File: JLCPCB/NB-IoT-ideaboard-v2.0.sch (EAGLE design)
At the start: 111 parts, among them Q1 32.768kHz, Q3 9013, Q4 9013, Q5 9013, U1 STM32F103RBT6, U2 MCP73831T-2ACI/OT, U3 AP2112-3.3, U4 PAM2401, U5 MICROSIM, U6 BC92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

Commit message: JLCPCB layout finished
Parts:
- removed C37: 100uF, rcl:C-EUC1210
- removed DEBUG: (no value), pinhead:PINHD-1X3
- removed S5: DTSM-6, switch-tact:DTSM-6
- removed U8: USBLC6-2SC6YSOT23-6L_STM-L, USBLC6:USBLC6-2SC6YSOT23-6L_STM-L
- added JP1: (no value), pinhead-2:PINHD-1X03_2.54-S
- added JP2: (no value), pinhead-2:PINHD-1X05_2.54-S
- added R31: 1k5, rcl:R-EU_R0805
- added S4: SWITCH-MOMENTARY-2SMD, SparkFun-Electromechanical:SWITCH-MOMENTARY-2SMD
- BOOT: device pinhead-2:PINHD-2X03_2.54-SMD -> pinhead-2:PINHD-2X03_2.54
- C10, C11: value 20pF -> 30pF
- C12, C13: value 4p3 -> 15pF
- C15: value 10uF -> 1uF
- C19: value 100nF -> 100uF; device rcl:C-EUC0805 -> rcl:CPOL-EUB/3528-21R
- C23: device Adafruit111:CAP_CERAMIC_0805 -> rcl:C-EUC0805
- CC1101, MODEMCTL: device pinhead-2:PINHD-2X05_2.54-SMD -> pinhead-2:PINHD-2X05_2.54
- L1: value 39nH -> 33nH; device wuerth-elektronik:WE-CBF_0805 -> wuerth-elektronik:WE-CBF_0603
- LIPO: value (none) -> C265329
- NET: device led:LEDCHIPLED_0805 -> led:LEDCHIP-LED0805
- R6: value 5k76 -> 5k6
- S2, S3, S6: value DTSM-6 -> SWITCH-MOMENTARY-2SMD; device switch-tact:DTSM-6 -> SparkFun-Electromechanical:SWITCH-MOMENTARY-2SMD
- renumbered PWR1 to LED
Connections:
- net PA11 renamed CAN_RX
- net PA12 renamed CAN_TX
- removed net N$15: F1.2, POWER.VBUS
- removed net N$29: MODEMCTL.8, R5.2
- removed net USB_CONN_D_N: POWER.D-, U8.I/O1_2
- removed net USB_CONN_D_P: POWER.D+, U8.I/O2_2
- removed net USB_D_N: U8.I/O1
- new net N$12: MODEMCTL.10, R5.2
- new net PC11: DIGITAL.5, U1A.PC11
- new net PC12: DIGITAL.2, U1A.PC12
- new net PC3: ANALOG.3, U1A.PC3
- new net PC6: JP2.2, U1A.PC6
- new net PC8: JP2.4, U1A.PC8
- new net PC9: JP2.5, U1A.PC9
- new net VIN: F1.2, POWER.VBUS, U$1.TIP
- net +3V3: now also R31.1; no longer C19.2, USART1.4
- net BC92_PWRKEY: now also S3.2; no longer S5.3, S5.4
- net BC92_RESET: now also C23.2, S6.2; no longer C23.1, S6.3, S6.4
- net BC92_TX: now also MODEMCTL.8; no longer MODEMCTL.10
- net DBG_RXD: now also JP1.2; no longer DEBUG.2
- net DBG_TXD: now also JP1.3; no longer DEBUG.3
- net GND: now also C19.-, C23.1, JP1.1, JP2.1, S4.1; no longer C19.1, C23.2, C37.2, DEBUG.1, S2.2, S3.2, S5.1, S5.2, S6.2, U8.GND
- net I2C1_SCL: now also I2C1.3; no longer I2C1.2
- net I2C1_SDA: now also I2C1.2; no longer I2C1.3
- net JTDO/SWO: no longer DIGITAL.5
- net NRST: now also S2.2; no longer S3.3, S3.4
- net PA2: now also DIGITAL.8; no longer DIGITAL.7
- net PA3: now also DIGITAL.7; no longer DIGITAL.8
- net PA4: no longer ANALOG.4
- net PB0: now also ANALOG.4; no longer ANALOG.3
- net PB12: no longer DIGITAL.2
- net PC13: now also S4.2; no longer S2.3, S2.4
- net PC7: now also JP2.3
- net STM_RX: now also MODEMCTL.7; no longer MODEMCTL.9
- net STM_TX: now also MODEMCTL.9; no longer MODEMCTL.7
- net USB_D_P: now also R31.2; no longer U8.I/O2
- net V+: now also C19.+; no longer C37.1
- net VBUS: now also USART1.4; no longer U$1.TIP, U8.VBUS
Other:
- moved on the sheet: C22, C23, CAN, L1, R19, R23, R5, R6, SPI2, SWD, USART1

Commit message: JLCPCB layout antenna layout edits
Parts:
- added JP3: (no value), pinhead-2:PINHD-1X01_2.54-S
- added POWER-PINS: (no value), pinhead-2:PINHD-1X04_2.54-S
- added Q2: 9013, discrete:TRANSISTOR-NPN-SOT23
- added R32: 1k, rcl:R-EU_R0805
- added R33: 47k, rcl:R-EU_R0805
- added R34: 4k7, rcl:R-EU_R0805
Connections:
- new net N$17: MODEMCTL.8, R32.2
- new net N$23: Q2.B, R33.1, R34.1
- new net PSM_EINT: MODEMCTL.2, R34.2
- net +3V3: now also JP3.1, POWER-PINS.2
- net +5V: now also POWER-PINS.3
- net BC92_PSM_EINT: now also Q2.C; no longer MODEMCTL.2
- net BC92_TX: now also R32.1; no longer MODEMCTL.8
- net GND: now also POWER-PINS.1, Q2.E, R33.2
- net VBUS: now also POWER-PINS.4
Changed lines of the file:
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@@
 <clearance class="4" value="0.2032"/>
 </class>
-<class number="5" name="antenna" width="0.3048" drill="0.3556">
-<clearance class="5" value="0.6096"/>
+<class number="5" name="antenna" width="0.8" drill="0.3556">
+<clearance class="5" value="0.15"/>
 </class>
 <class number="6" name="usb_diff" width="0.254" drill="0.3556">
@@
 <part name="S3" library="SparkFun-Electromechanical" deviceset="SWITCH-MOMENTARY-2" device="SMD"/>
 <part name="S6" library="SparkFun-Electromechanical" deviceset="SWITCH-MOMENTARY-2" device="SMD"/>
+<part name="POWER-PINS" library="pinhead-2" deviceset="PINHD-1X04" device="_2.54-S"/>
+<part name="GND13" library="supply1" deviceset="GND" device=""/>
+<part name="+3V1" library="supply1" deviceset="+3V3" device=""/>
+<part name="V3" library="Adafruit111" deviceset="VBUS" device=""/>
+<part name="P+1" library="supply1" deviceset="+5V" device=""/>
+<part name="JP3" library="pinhead-2" deviceset="PINHD-1X01" device="_2.54-S"/>
+<part name="+3V11" library="supply1" deviceset="+3V3" device=""/>
+<part name="R32" library="rcl" library_urn="urn:adsk.eagle:library:334" deviceset="R-EU_" device="R0805" package3d_urn="urn:adsk.eagle:package:23553/2" value="1k"/>
+<part name="Q2" library="discrete" deviceset="TRANSISTOR-NPN*" device="-SOT23" value="9013"/>
+<part name="GND55" library="supply1" deviceset="GND" device=""/>
+<part name="R33" library="rcl" library_urn="urn:adsk.eagle:library:334" deviceset="R-EU_" device="R0805" package3d_urn="urn:adsk.eagle:package:23553/2" value="47k"/>
+<part name="R34" library="rcl" library_urn="urn:adsk.eagle:library:334" deviceset="R-EU_" device="R0805" package3d_urn="urn:adsk.eagle:package:23553/2" value="4k7"/>
 </parts>
 <sheets>
@@
 <attribute name="VALUE" x="177.8" y="120.65" size="1.778" layer="96"/>
 </instance>
-<instance part="S4" gate="G$1" x="72.39" y="46.99" rot="R90"/>
-<instance part="S2" gate="G$1" x="177.8" y="52.07" rot="R90"/>
+<instance part="S4" gate="G$1" x="72.39" y="46.99" smashed="yes" rot="R90">
+<attribute name="NAME" x="69.85" y="44.45" size="1.778" layer="95" rot="R90"/>
+</instance>
+<instance part="S2" gate="G$1" x="177.8" y="52.07" smashed="yes" rot="R90">
+<attribute name="NAME" x="175.26" y="49.53" size="1.778" layer="95" rot="R90"/>
+</instance>
+<instance part="R32" gate="G$1" x="161.29" y="76.2" rot="R180"/>
 </instances>
 <busses>
@@
 <net name="BC92_TX" class="0">
 <segment>
-<wire x1="152.4" y1="76.2" x2="172.72" y2="76.2" width="0.1524" layer="91"/>
+<wire x1="166.37" y1="76.2" x2="172.72" y2="76.2" width="0.1524" layer="91"/>
 <label x="172.72" y="76.2" size="1.27" layer="95" xref="yes"/>
-<pinref part="MODEMCTL" gate="A" pin="8"/>
+<pinref part="R32" gate="G$1" pin="1"/>
 </segment>
 </net>
@@
 <wire x1="168.91" y1="73.66" x2="172.72" y2="73.66" width="0.1524" layer="91"/>
 <junction x="168.91" y="73.66"/>
-</segment>
-</net>
-<net name="BC92_PSM_EINT" class="0">
-<segment>
-<wire x1="152.4" y1="83.82" x2="172.72" y2="83.82" width="0.1524" layer="91"/>
-<label x="172.72" y="83.82" size="1.27" layer="95" xref="yes"/>
-<pinref part="MODEMCTL" gate="A" pin="2"/>
 </segment>
 </net>
@@
 <wire x1="95.25" y1="111.76" x2="100.33" y2="111.76" width="0.1524" layer="91"/>
 <label x="100.33" y="111.76" size="1.27" layer="95" xref="yes"/>
+</segment>
+</net>
+<net name="N$17" class="0">
+<segment>
+<pinref part="R32" gate="G$1" pin="2"/>
+<pinref part="MODEMCTL" gate="A" pin="8"/>
+<wire x1="156.21" y1="76.2" x2="152.4" y2="76.2" width="0.1524" layer="91"/>
+</segment>
+</net>
+<net name="PSM_EINT" class="0">
+<segment>
+<wire x1="152.4" y1="83.82" x2="172.72" y2="83.82" width="0.1524" layer="91"/>
+<label x="172.72" y="83.82" size="1.27" layer="95" xref="yes"/>
+<pinref part="MODEMCTL" gate="A" pin="2"/>
 </segment>
 </net>
@@
 <instance part="JP1" gate="A" x="127" y="41.91" rot="R180"/>
 <instance part="JP2" gate="A" x="128.27" y="87.63" rot="R180"/>
+<instance part="POWER-PINS" gate="A" x="128.27" y="116.84" rot="R180"/>
+<instance part="GND13" gate="1" x="138.43" y="107.95"/>
+<instance part="+3V1" gate="G$1" x="140.97" y="128.27" smashed="yes">
+<attribute name="VALUE" x="142.24" y="128.27" size="1.778" layer="96"/>
+</instance>
+<instance part="V3" gate="G$1" x="147.32" y="128.27"/>
+<instance part="P+1" gate="1" x="154.94" y="128.27"/>
+<instance part="JP3" gate="A" x="128.27" y="97.79" rot="R180"/>
+<instance part="+3V11" gate="G$1" x="142.24" y="104.14" smashed="yes">
+<attribute name="VALUE" x="143.51" y="104.14" size="1.778" layer="96"/>
+</instance>
 </instances>
 <busses>
@@
 <pinref part="I2C1" gate="A" pin="1"/>
 </segment>
+<segment>
+<pinref part="POWER-PINS" gate="A" pin="2"/>
+<pinref part="+3V1" gate="G$1" pin="+3V3"/>
+<wire x1="130.81" y1="114.3" x2="140.97" y2="114.3" width="0.1524" layer="91"/>
+<wire x1="140.97" y1="114.3" x2="140.97" y2="125.73" width="0.1524" layer="91"/>
+</segment>
+<segment>
+<pinref part="JP3" gate="A" pin="1"/>
+<wire x1="130.81" y1="97.79" x2="142.24" y2="97.79" width="0.1524" layer="91"/>
+<wire x1="142.24" y1="97.79" x2="142.24" y2="101.6" width="0.1524" layer="91"/>
+<pinref part="+3V11" gate="G$1" pin="+3V3"/>
+</segment>
 </net>
 <net name="GND" class="2">
@@
 <pinref part="JP2" gate="A" pin="1"/>
 </segment>
+<segment>
+<pinref part="POWER-PINS" gate="A" pin="1"/>
+<pinref part="GND13" gate="1" pin="GND"/>
+<wire x1="130.81" y1="111.76" x2="138.43" y2="111.76" width="0.1524" layer="91"/>
+<wire x1="138.43" y1="111.76" x2="138.43" y2="110.49" width="0.1524" layer="91"/>
+</segment>
 </net>
 <net name="PA6" class="0">
@@
 <pinref part="V5" gate="G$1" pin="VBUS"/>
 </segment>
+<segment>
+<pinref part="POWER-PINS" gate="A" pin="4"/>
+<pinref part="V3" gate="G$1" pin="VBUS"/>
+<wire x1="130.81" y1="119.38" x2="147.32" y2="119.38" width="0.1524" layer="91"/>
+<wire x1="147.32" y1="119.38" x2="147.32" y2="125.73" width="0.1524" layer="91"/>
+</segment>
 </net>
 <net name="PC6" class="0">
@@
 <wire x1="130.81" y1="92.71" x2="137.16" y2="92.71" width="0.1524" layer="91"/>
 <label x="137.16" y="92.71" size="1.27" layer="95" xref="yes"/>
+</segment>
+</net>
+<net name="+5V" class="3">
+<segment>
+<pinref part="POWER-PINS" gate="A" pin="3"/>
+<pinref part="P+1" gate="1" pin="+5V"/>
+<wire x1="130.81" y1="116.84" x2="154.94" y2="116.84" width="0.1524" layer="91"/>
+<wire x1="154.94" y1="116.84" x2="154.94" y2="125.73" width="0.1524" layer="91"/>
 </segment>
 </net>
@@
 <instance part="S3" gate="G$1" x="54.61" y="86.36" rot="R270"/>
 <instance part="S6" gate="G$1" x="53.34" y="41.91" rot="R270"/>
+<instance part="Q2" gate="G$1" x="158.75" y="160.02" smashed="yes">
+<attribute name="NAME" x="156.21" y="162.56" size="1.016" layer="95" ratio="10"/>
+<attribute name="VALUE" x="161.29" y="160.02" size="1.016" layer="96" ratio="10"/>
+</instance>
+<instance part="GND55" gate="1" x="154.94" y="140.97" smashed="yes" rot="MR0">
+<attribute name="VALUE" x="157.48" y="138.43" size="1.778" layer="96" rot="MR0"/>
+</instance>
+<instance part="R33" gate="G$1" x="154.94" y="153.67" rot="R270"/>
+<instance part="R34" gate="G$1" x="144.78" y="160.02" rot="R180"/>
 </instances>
 <busses>
@@
 <wire x1="77.47" y1="105.41" x2="77.47" y2="102.87" width="0.1524" layer="91"/>
 </segment>
+<segment>
+<pinref part="Q2" gate="G$1" pin="E"/>
+<wire x1="161.29" y1="154.94" x2="161.29" y2="147.32" width="0.1524" layer="91"/>
+<wire x1="161.29" y1="147.32" x2="154.94" y2="147.32" width="0.1524" layer="91"/>
+<wire x1="154.94" y1="147.32" x2="154.94" y2="148.59" width="0.1524" layer="91"/>
+<wire x1="154.94" y1="147.32" x2="154.94" y2="143.51" width="0.1524" layer="91"/>
+<junction x="154.94" y="147.32"/>
+<pinref part="GND55" gate="1" pin="GND"/>
+<pinref part="R33" gate="G$1" pin="2"/>
+</segment>
 </net>
 <net name="N$16" class="0">
@@
 <label x="144.78" y="54.61" size="1.27" layer="95" rot="R270" xref="yes"/>
 </segment>
+<segment>
+<wire x1="161.29" y1="165.1" x2="161.29" y2="166.37" width="0.1524" layer="91"/>
+<pinref part="Q2" gate="G$1" pin="C"/>
+<wire x1="161.29" y1="166.37" x2="165.1" y2="166.37" width="0.1524" layer="91"/>
+<label x="165.1" y="166.37" size="1.27" layer="95" xref="yes"/>
+</segment>
 </net>
 <net name="BC92_TX" class="0">
@@
 </segment>
 </net>
-<net name="N$6" class="0">
+<net name="N$6" class="5">
 <segment>
 <pinref part="RF_ANT" gate="G$1" pin="D"/>
@@
 </segment>
 </net>
+<net name="N$23" class="0">
+<segment>
+<pinref part="R34" gate="G$1" pin="1"/>
+<pinref part="Q2" gate="G$1" pin="B"/>
+<wire x1="149.86" y1="160.02" x2="154.94" y2="160.02" width="0.1524" layer="91"/>
+<pinref part="R33" gate="G$1" pin="1"/>
+<wire x1="154.94" y1="160.02" x2="156.21" y2="160.02" width="0.1524" layer="91"/>
+<wire x1="154.94" y1="158.75" x2="154.94" y2="160.02" width="0.1524" layer="91"/>
+<junction x="154.94" y="160.02"/>
+</segment>
+</net>
+<net name="PSM_EINT" class="0">
+<segment>
+<pinref part="R34" gate="G$1" pin="2"/>
+<wire x1="139.7" y1="160.02" x2="137.16" y2="160.02" width="0.1524" layer="91"/>
+<label x="137.16" y="160.02" size="1.27" layer="95" rot="R180" xref="yes"/>
+</segment>
+</net>

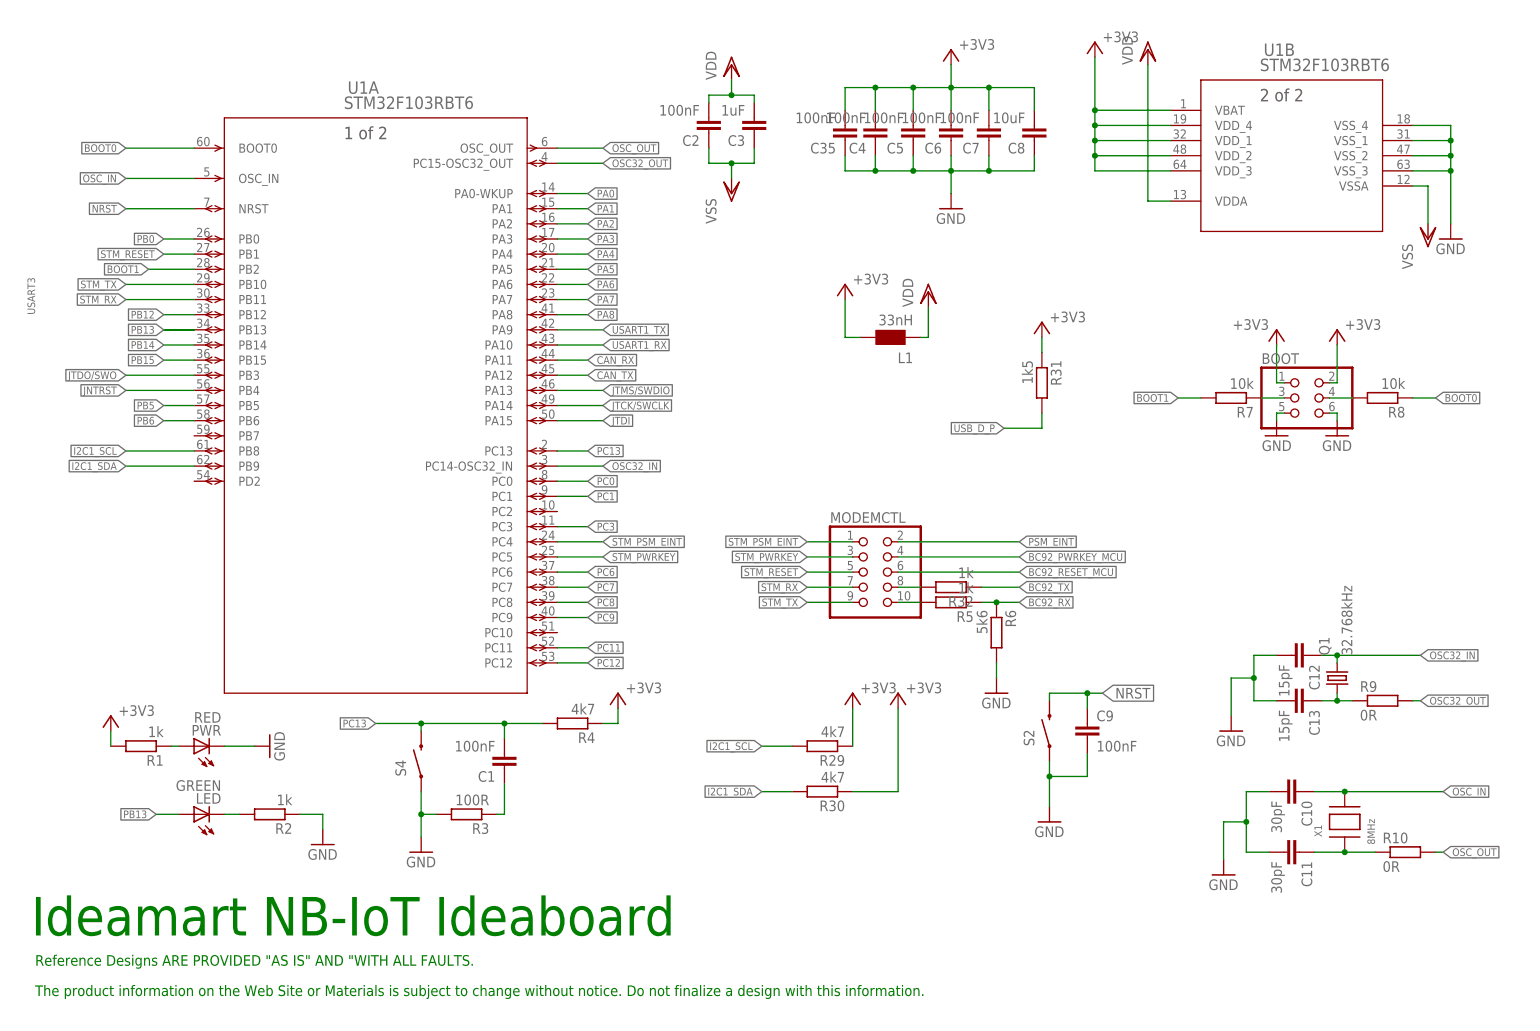
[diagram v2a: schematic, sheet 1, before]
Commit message: JLCPCB header position changes
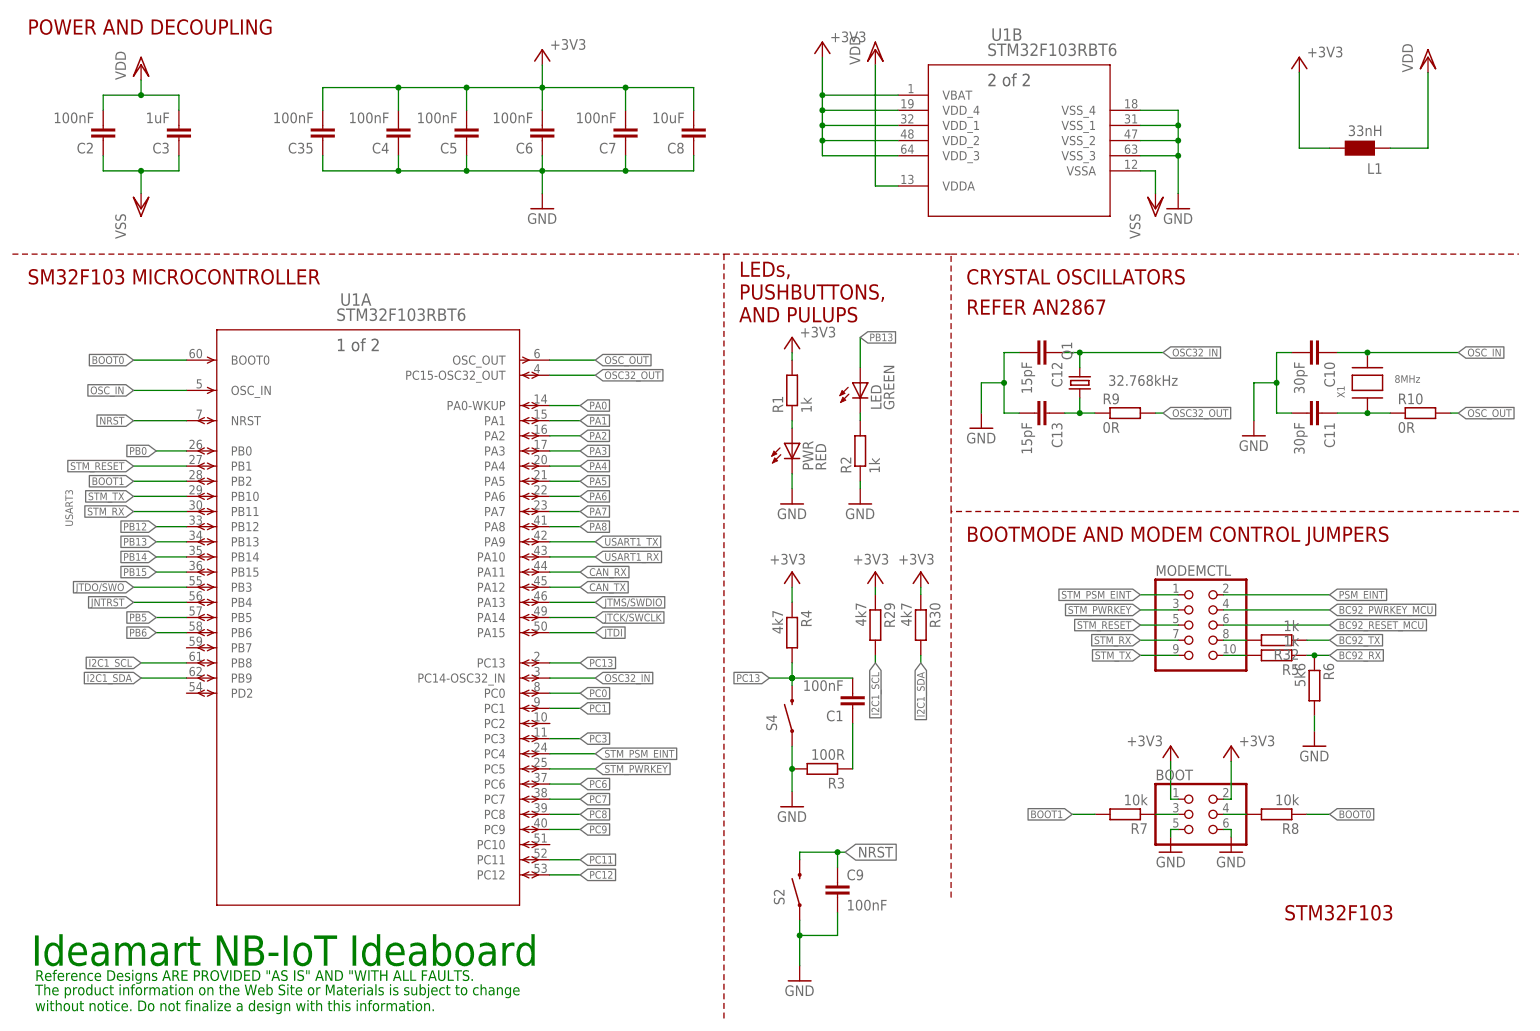
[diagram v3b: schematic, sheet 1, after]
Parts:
- removed R31: 1k5, rcl:R-EU_R0805
- added JP4: (no value), jumper:JP1E
- added POWER-PINS1: (no value), pinhead-2:PINHD-1X04_2.54-S
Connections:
- removed net USB_D_P: R31.2
- new net N$24: JP4.2, S1.O, S1.P
- net +3V3: now also POWER-PINS1.2, SWD.3; no longer R31.1, SWD.6
- net +4.1V: now also JP4.1; no longer S1.O, S1.P
- net +5V: now also POWER-PINS1.3
- net GND: now also POWER-PINS1.1, SWD.5; no longer SWD.4
- net JTCK/SWCLK: now also SWD.4; no longer SWD.5
- net JTMS/SWDIO: now also SWD.6; no longer SWD.3
- net VBUS: now also POWER-PINS1.4
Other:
- note added: "3.3V REGULATOR"
- note added: "5V STEPUP CONVERTER"
- note added: "BOOTMODE AND MODEM CONTROL JUMPERS"
- note added: "CONNECTORS AND POWER SWITCH"
- note added: "CRYSTAL OSCILLATORS"
- note added: "INDICATORS & PUSHBUTTONS"
- note added: "LEDs, PUSHBUTTONS, AND PULUPS"
- note added: "LIPO BATTERY CHARGING"
- note added: "PINHEADERS"
- note added: "POWER AND DECOUPLING"
- note added: "POWER DECOUPLING AND EMI SUPRESSION"
- note added: "POWER SUPPLY"
- note added: "QUECTEL BC92"
- note added: "QUECTEL BC92 MODULE"
- note added: "REFER AN2867"
- note added: "SM32F103 MICROCONTROLLER"
- note added: "STM32F103"
- note added: "eSIM AND MICROSIM CONNECTOR"
- note removed: "3.3V VOLTAGE REGULATION"
- note removed: "DC POWER INPUT"
- note removed: "LIPO CHARGE CONTROLLER"
- note removed: "MICROSIM CONNECTOR"
- note removed: "NETLIGHT"
- note removed: "POWERSUPPLY DECOUPLING"
- note removed: "PWRKEY AND RESET BUTTONS"
- note removed: "SIM7000 NB-IoT Module"
- note removed: "Switching Regulator"
- note removed: "TVS ARRAY"
- note removed: "USB to Serial - FT232RL"
- moved on the sheet: ANALOG, BOOT, C1, C10, C11, C12, C13, C14, C15, C16, C17, C18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

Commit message: Adds USB FS data lines for CDC Virtual Com port
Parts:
- added R31: 1k5, rcl:R-EU_R0805
- added U8: USBLC6-2SC6YSOT23-6L_STM-L, USBLC6:USBLC6-2SC6YSOT23-6L_STM-L
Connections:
- removed net CAN_RX: CAN.3, U1A.PA11
- removed net CAN_TX: CAN.2, U1A.PA12
- removed net VSS: C2.1, C3.1, U1B.VSSA
- new net USB_CONN_D_N: POWER.D-, U8.I/O1_2
- new net USB_CONN_D_P: POWER.D+, U8.I/O2_2
- new net USB_D_N: CAN.3, U1A.PA11, U8.I/O1
- new net USB_D_P: CAN.2, R31.2, U1A.PA12, U8.I/O2
- net +3V3: now also R31.1
- net GND: now also C2.1, C3.1, U1B.VSSA, U8.GND
- net VBUS: now also U8.VBUS
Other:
- moved on the sheet: C9, F1, JP4, POWER, S1, S2, U$1
